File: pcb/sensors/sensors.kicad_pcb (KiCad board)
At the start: 2 copper layers, 33 x 70 mm, 27 parts, among them J1 5V POWER, J3 CAN BUS, J4 DIMMER I2C, J5 DIMMER I2C, J6 FLOW HALL, J7 VALVE SSR, J8 BOILER SSR, Q2 AO3401A, Q3 2N7002, U1 XIAO ESP32-S3 / SOCKETED, U4 TJA1051T/3, U5 TMP102AIDRLR

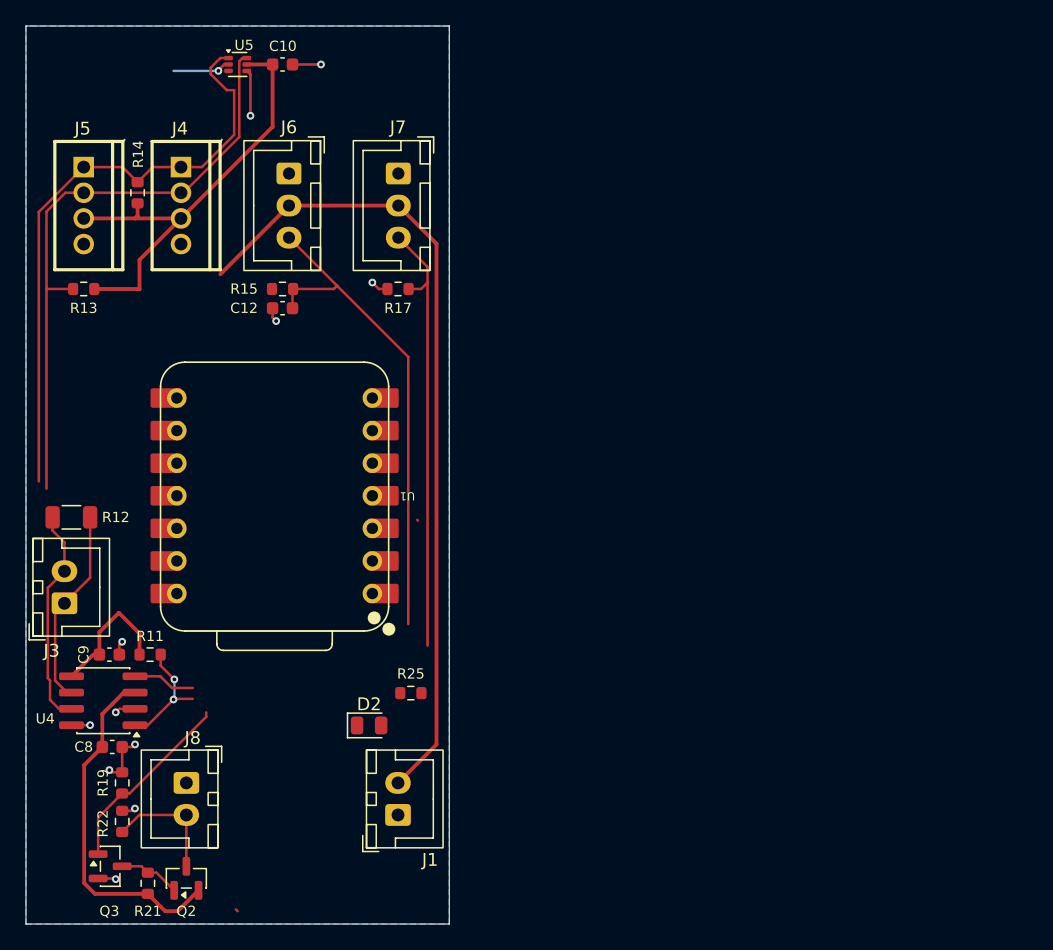
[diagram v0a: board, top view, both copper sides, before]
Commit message: Route the sensors board and add the accontrol and pressure inputs
Finish the sensors PCB routing. Give the XIAO a local footprint that keeps
only the header holes (1.0 mm drill) with one courtyard per header, so parts
can sit under the module.

Add J9 (XH 5, accontrol J1 order) with ZC on GPIO1 and DIM_CMD on GPIO3, and
an optional ADS1115 (U6, 0x49) with J10 and the screen_sensors pressure
filter. Record why the CAN terminator R12 is a 1206.

Co-Authored-By: Claude Opus 5.5 <noreply@anthropic.com>
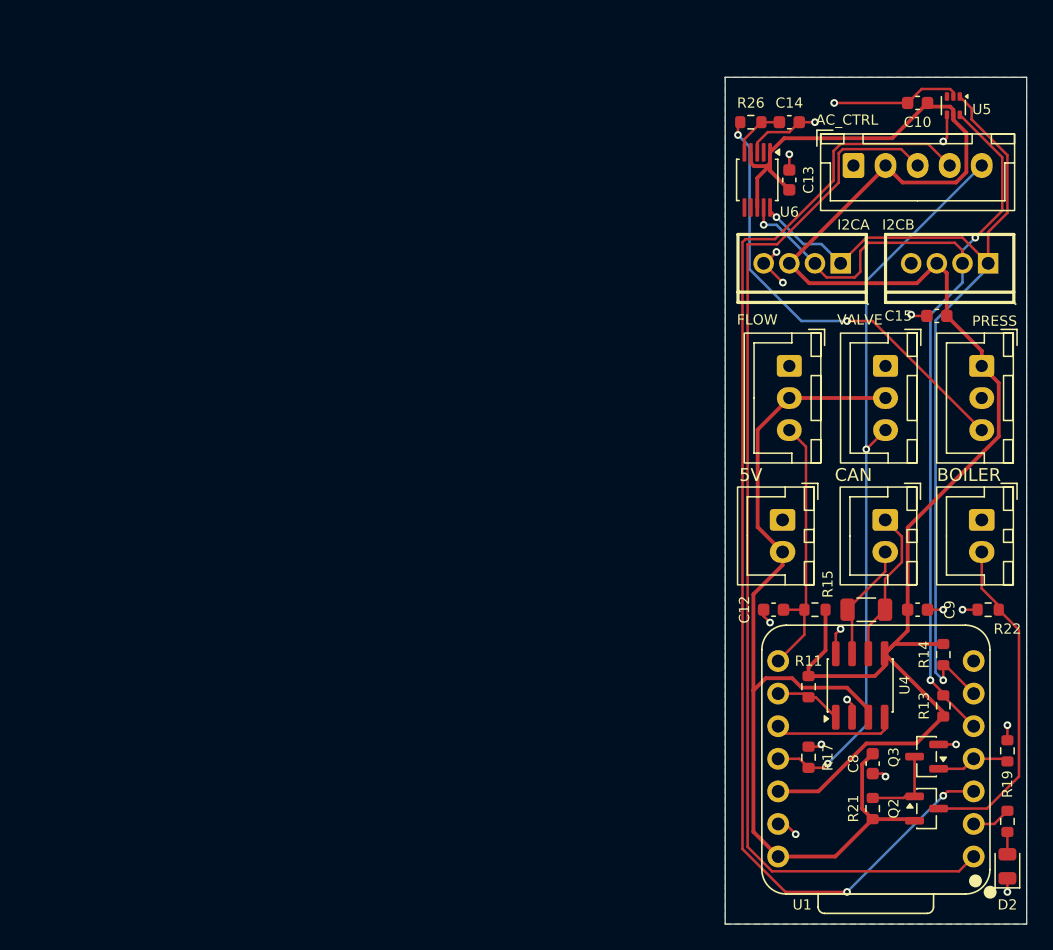
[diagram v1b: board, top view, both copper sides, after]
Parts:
- added AC_CTRL: AC CONTROL, Connector_JST:JST_XH_B5B-XH-A_1x05_P2.50mm_Vertical, F.Cu at (219.5, 90.9)
- added C13: 100nF, Capacitor_SMD:C_0603_1608Metric, F.Cu at (214.5, 92.0)
- added C14: 10uF, Capacitor_SMD:C_0603_1608Metric, F.Cu at (214.5, 87.5)
- added C15: 100nF, Capacitor_SMD:C_0603_1608Metric, F.Cu at (226.0, 102.6)
- added PRESS: PRESSURE, Connector_JST:JST_XH_B3B-XH-A_1x03_P2.50mm_Vertical, F.Cu at (229.5, 106.5)
- added R26: 1k, Resistor_SMD:R_0603_1608Metric, F.Cu at (211.5, 87.5)
- added U6: ADS1115IDGSR, Package_SO:TSSOP-10_3x3mm_P0.5mm, F.Cu at (212.0, 92.0)
- U1: footprint Seeed_XIAO:XIAO-ESP32-S3-DIP -> Sensors_Local:XIAO-ESP32-S3-DIP-Headers
- moved R13 74.5 mm to (226.5, 133.0), turned to 90 degrees
- moved R14 72.4 mm to (226.5, 129.0), turned to -90 degrees
- moved R22 69.5 mm to (230.0, 125.5), turned to 180 degrees
- moved R19 69.0 mm to (231.5, 136.5)
- moved BOILER 65.3 mm to (229.5, 118.5)
- moved CAN 64.3 mm to (222.0, 118.5), turned to -90 degrees
- moved Q3 64.2 mm to (225.2, 136.9), turned to 180 degrees
- moved I2CB 63.4 mm to (230.0, 98.5), turned to -90 degrees
- moved C9 63.1 mm to (224.5, 125.5)
- moved R12 62.4 mm to (220.5, 125.5)
- moved I2CA 59.5 mm to (218.5, 98.5), turned to -90 degrees
- moved C8 59.3 mm to (221.0, 137.5), turned to -90 degrees
- moved U4 59.0 mm to (220.0, 131.4), turned to 90 degrees
- moved Q2 58.0 mm to (225.2, 141.0), turned to 0 degrees
- moved R21 56.8 mm to (221.0, 141.0)
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- renumbered J1 to 5V, J8 to BOILER, J3 to CAN, J6 to FLOW, J5 to I2CA, J4 to I2CB, J7 to VALVE
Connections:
- U1 pad 1: unconnected-(U1-D0-Pad1) -> ZC
- U1 pad 3: unconnected-(U1-D2-Pad3) -> DIM_CMD
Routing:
- net +3V3: track 46.9 -> 139.7 mm
- net DIM_CMD: track 0.00 -> 91.3 mm, vias 0 -> 2
- net ZC: track 0.00 -> 84.1 mm
- net PRESSURE: track 0.00 -> 35.2 mm, vias 0 -> 2
- net I2C_SDA: track 47.7 -> 74.7 mm, vias 0 -> 3
- net I2C_SCL: track 47.7 -> 74.7 mm, vias 0 -> 2
- net VALVE_CMD: track 34.4 -> 58.0 mm, vias 0 -> 2
- net FLOW_PULSE: track 39.0 -> 21.1 mm
- net +5V: track 92.7 -> 75.5 mm
- net /Sensors interfaces/BOILER_5V: track 9.80 -> 26.0 mm
- net GND: track 23.9 -> 39.7 mm, vias 12 -> 18
- net HEATER_CMD: track 14.9 -> 5.77 mm
- net /Sensors interfaces/CAN_H: track 17.2 -> 9.29 mm
- net CAN_RX: track 3.88 -> 9.64 mm
- net PRESSURE_ADC: track 0.00 -> 4.30 mm
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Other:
- board size 33 x 70 mm -> 23.5 x 66 mm

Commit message: Swap ZC and DIM_CMD on the XIAO to ease routing
DIM_CMD moves to GPIO1 (pin 1) and ZC to GPIO3 (pin 3). GPIO3 only acts as
a strapping pin once STRAP_JTAG_SEL is burned, so the ZC level at reset is
harmless; accontrol's pull-down still keeps DIM low during boot.

Co-Authored-By: Claude Opus 5.5 <noreply@anthropic.com>
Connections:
- U1 pad 1: ZC -> DIM_CMD
- U1 pad 3: DIM_CMD -> ZC
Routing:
- net ZC: track 84.1 -> 89.8 mm
- net DIM_CMD: track 91.3 -> 89.2 mm, vias 2 -> 0

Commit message: Remove the accontrol connector J9 from the sensors board
The AC control board is shelved, so the valve and pump stay on the M5Stack
SSR (J7) and the RobotDyn dimmer (Grove I2C). Drop J9 and its wiring, and
leave D0/GPIO1 and D2/GPIO3 of the XIAO unconnected. The design notes say
how a future single AC board would take over from the dimmer I2C and J7.

The connectors now keep their J references on the PCB, hidden, with board
text labels for their functions.

Co-Authored-By: Claude Opus 5.5 <noreply@anthropic.com>
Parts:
- removed AC_CTRL: AC CONTROL, Connector_JST:JST_XH_B5B-XH-A_1x05_P2.50mm_Vertical
- moved C13 7.91 mm to (222.0, 94.5), turned to -90 degrees
- moved C10 6.96 mm to (226.7, 92.6)
- moved U5 6.31 mm to (229.5, 92.1)
- moved U6 6.08 mm to (218.0, 93.0), turned to 0 degrees
- moved C14 5.70 mm to (213.0, 93.0), turned to -90 degrees
- moved R26 5.50 mm to (211.5, 93.0), turned to 90 degrees
- renumbered 5V to J1, PRESS to J10, CAN to J3, I2CB to J4, I2CA to J5, FLOW to J6, VALVE to J7, BOILER to J8
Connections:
- U1 pad 1: DIM_CMD -> unconnected-(U1-D0-Pad1)
- U1 pad 3: ZC -> unconnected-(U1-D2-Pad3)
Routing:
- net ZC: track 89.8 -> 0.00 mm
- net DIM_CMD: track 89.2 -> 0.00 mm
- net +3V3: track 139.7 -> 113.8 mm
- net VALVE_CMD: track 58.0 -> 32.2 mm
- net PRESSURE: track 35.2 -> 28.5 mm, vias 2 -> 0
- net I2C_SCL: track 74.7 -> 68.2 mm
- net GND: track 39.7 -> 33.3 mm, vias 18 -> 17
- net I2C_SDA: track 74.7 -> 69.7 mm
- net PRESSURE_ADC: track 4.30 -> 5.11 mm
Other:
- board size 23.5 x 66 mm -> 23.5 x 60 mm
- board text added: "BOILER"
- board text added: "CAN"
- board text added: "FLOW"
- board text added: "I2C A"
- board text added: "I2C B"
- board text added: "POWER 5V"
- board text added: "PRESS"
- board text added: "VALVE"
